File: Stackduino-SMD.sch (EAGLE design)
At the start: 58 parts

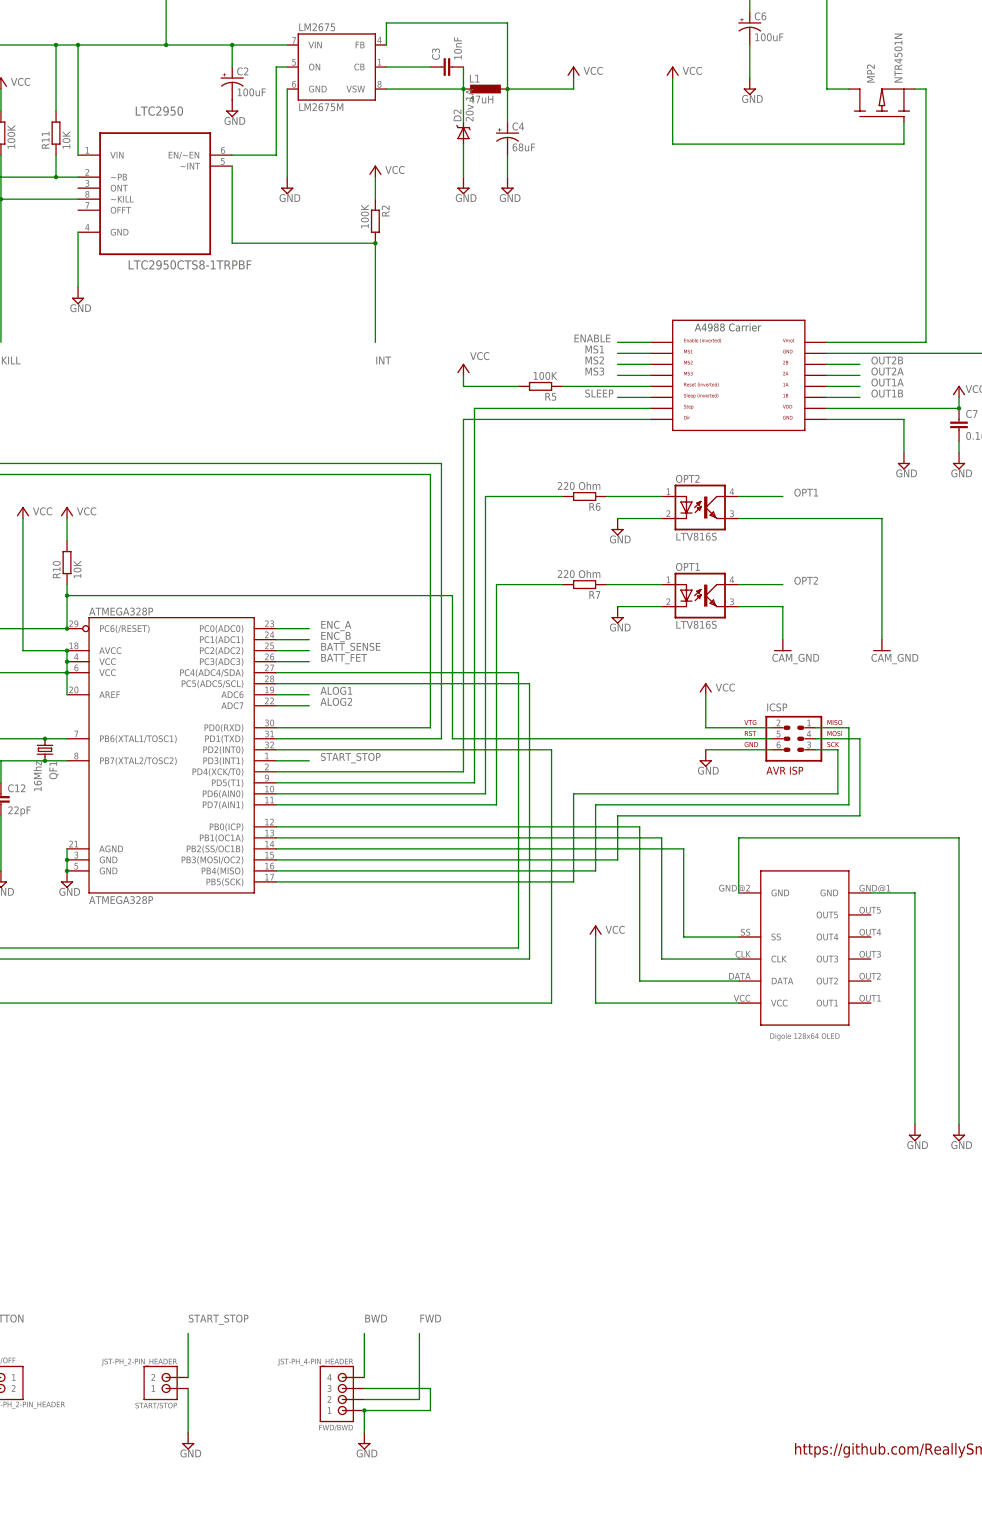
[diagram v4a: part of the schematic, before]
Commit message: reorganised traces to avoid inductor
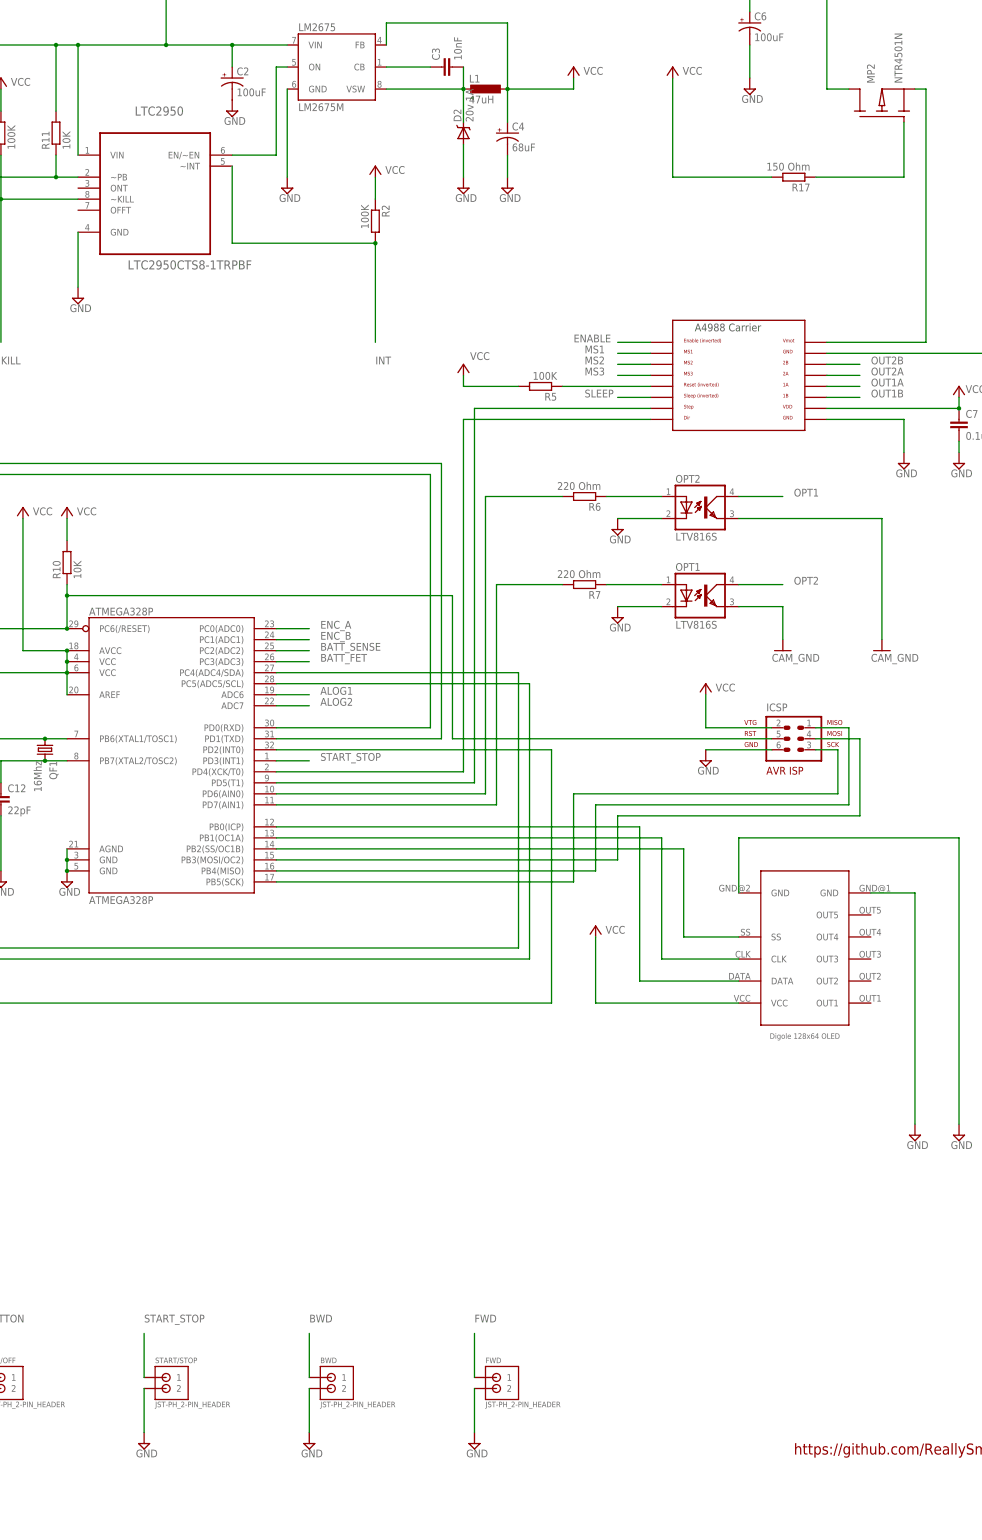
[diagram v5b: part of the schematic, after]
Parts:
- removed FWD/BWD: JST-PH_4-PIN_HEADER, SRG:JST-PH_4-PIN_HEADER
- added BWD, FWD: JST-PH_2-PIN_HEADER, SRG:JST-PH_2-PIN_HEADER
- added R17: 150 Ohm, eagle-ltspice:R
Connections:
- new net N$10: MP2.G, R17.1
- net BWD: now also BWD.1; no longer FWD/BWD.4
- net FWD: now also FWD.1; no longer FWD/BWD.2
- net GND: now also BWD.2, FWD.2, START/STOP.2; no longer FWD/BWD.1, FWD/BWD.3, START/STOP.1
- net START_STOP: now also START/STOP.1; no longer START/STOP.2
- net VCC: now also R17.2; no longer MP2.G
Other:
- moved on the sheet: START/STOP
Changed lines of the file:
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@@
 <part name="SUPPLY29" library="supply2" deviceset="GND" device=""/>
 <part name="SUPPLY30" library="supply2" deviceset="GND" device=""/>
-<part name="SUPPLY33" library="supply2" deviceset="GND" device=""/>
 <part name="SUPPLY35" library="supply2" deviceset="GND" device=""/>
 <part name="SUPPLY36" library="supply2" deviceset="GND" device=""/>
@@
 <part name="ENCODER" library="SRG" deviceset="JST-PH_3-PIN_HEADER" device=""/>
 <part name="MENU_SEL" library="SRG" deviceset="JST-PH_2-PIN_HEADER" device=""/>
-<part name="FWD/BWD" library="SRG" deviceset="JST-PH_4-PIN_HEADER" device=""/>
 <part name="ON/OFF" library="SRG" deviceset="JST-PH_2-PIN_HEADER" device=""/>
 <part name="R1" library="eagle-ltspice" deviceset="R" device="" value="100K"/>
@@
 <part name="CAM_GND2" library="supply1" deviceset="GND" device="" value="CAM_GND"/>
 <part name="FRAME1" library="frames" deviceset="FRAME_C_L" device=""/>
+<part name="BWD" library="SRG" deviceset="JST-PH_2-PIN_HEADER" device=""/>
+<part name="FWD" library="SRG" deviceset="JST-PH_2-PIN_HEADER" device=""/>
+<part name="SUPPLY19" library="supply2" deviceset="GND" device=""/>
+<part name="SUPPLY23" library="supply2" deviceset="GND" device=""/>
+<part name="R17" library="eagle-ltspice" deviceset="R" device="" value="150 Ohm"/>
 </parts>
 <sheets>
@@
 <instance part="ICSP" gate="G$1" x="129.54" y="-17.78"/>
 <instance part="SUPPLY24" gate="GND" x="109.22" y="-22.86"/>
-<instance part="SUPPLY26" gate="GND" x="-10.16" y="-180.34"/>
+<instance part="SUPPLY26" gate="GND" x="-20.32" y="-180.34"/>
 <instance part="SUPPLY27" gate="GND" x="-91.44" y="-180.34"/>
 <instance part="SUPPLY29" gate="GND" x="88.9" y="10.16"/>
 <instance part="SUPPLY30" gate="GND" x="88.9" y="30.48"/>
-<instance part="SUPPLY33" gate="GND" x="30.48" y="-180.34"/>
 <instance part="SUPPLY35" gate="GND" x="-215.9" y="-180.34"/>
 <instance part="SUPPLY36" gate="GND" x="-200.66" y="-180.34"/>
@@
 <instance part="C1" gate="G$1" x="-78.74" y="134.62"/>
 <instance part="GND4" gate="GND" x="-78.74" y="91.44"/>
-<instance part="START/STOP" gate="G$1" x="-17.78" y="-165.1" rot="R180"/>
+<instance part="START/STOP" gate="G$1" x="-12.7" y="-167.64"/>
 <instance part="ENCODER" gate="G$1" x="-99.06" y="-167.64" rot="R180"/>
 <instance part="MENU_SEL" gate="G$1" x="-132.08" y="-167.64"/>
-<instance part="FWD/BWD" gate="G$1" x="22.86" y="-170.18" rot="R180"/>
 <instance part="ON/OFF" gate="G$1" x="-50.8" y="-167.64"/>
 <instance part="R1" gate="G$1" x="-53.34" y="121.92" rot="R90"/>
@@
 <instance part="FRAME1" gate="G$1" x="-325.12" y="-210.82"/>
 <instance part="FRAME1" gate="G$2" x="127" y="-210.82"/>
+<instance part="BWD" gate="G$1" x="25.4" y="-167.64"/>
+<instance part="FWD" gate="G$1" x="63.5" y="-167.64"/>
+<instance part="SUPPLY19" gate="GND" x="17.78" y="-180.34"/>
+<instance part="SUPPLY23" gate="GND" x="55.88" y="-180.34"/>
+<instance part="R17" gate="G$1" x="129.54" y="111.76" rot="R180"/>
 </instances>
 <busses>
@@
 </segment>
 <segment>
-<pinref part="START/STOP" gate="G$1" pin="1"/>
 <pinref part="SUPPLY26" gate="GND" pin="GND"/>
-<wire x1="-10.16" y1="-167.64" x2="-10.16" y2="-177.8" width="0.1524" layer="91"/>
-</segment>
-<segment>
-<pinref part="SUPPLY33" gate="GND" pin="GND"/>
-<pinref part="FWD/BWD" gate="G$1" pin="1"/>
-<wire x1="30.48" y1="-177.8" x2="30.48" y2="-172.72" width="0.1524" layer="91"/>
-<pinref part="FWD/BWD" gate="G$1" pin="3"/>
-<wire x1="30.48" y1="-167.64" x2="45.72" y2="-167.64" width="0.1524" layer="91"/>
-<wire x1="45.72" y1="-167.64" x2="45.72" y2="-172.72" width="0.1524" layer="91"/>
-<wire x1="45.72" y1="-172.72" x2="30.48" y2="-172.72" width="0.1524" layer="91"/>
-<junction x="30.48" y="-172.72"/>
+<pinref part="START/STOP" gate="G$1" pin="2"/>
+<wire x1="-20.32" y1="-167.64" x2="-20.32" y2="-177.8" width="0.1524" layer="91"/>
 </segment>
 <segment>
@@
 <wire x1="-208.28" y1="96.52" x2="-208.28" y2="71.12" width="0.1524" layer="91"/>
 <pinref part="SUPPLY13" gate="GND" pin="GND"/>
+</segment>
+<segment>
+<pinref part="SUPPLY19" gate="GND" pin="GND"/>
+<pinref part="BWD" gate="G$1" pin="2"/>
+<wire x1="17.78" y1="-167.64" x2="17.78" y2="-177.8" width="0.1524" layer="91"/>
+</segment>
+<segment>
+<pinref part="SUPPLY23" gate="GND" pin="GND"/>
+<pinref part="FWD" gate="G$1" pin="2"/>
+<wire x1="55.88" y1="-167.64" x2="55.88" y2="-177.8" width="0.1524" layer="91"/>
 </segment>
 </net>
@@
 </segment>
 <segment>
-<pinref part="START/STOP" gate="G$1" pin="2"/>
-<wire x1="-10.16" y1="-154.94" x2="-10.16" y2="-165.1" width="0.1524" layer="91"/>
-<label x="-10.16" y="-152.4" size="1.778" layer="95"/>
+<label x="-20.32" y="-152.4" size="1.778" layer="95"/>
+<pinref part="START/STOP" gate="G$1" pin="1"/>
+<wire x1="-20.32" y1="-165.1" x2="-20.32" y2="-154.94" width="0.1524" layer="91"/>
 </segment>
 </net>
@@
 <net name="FWD" class="0">
 <segment>
-<pinref part="FWD/BWD" gate="G$1" pin="2"/>
-<wire x1="30.48" y1="-170.18" x2="43.18" y2="-170.18" width="0.1524" layer="91"/>
-<wire x1="43.18" y1="-170.18" x2="43.18" y2="-154.94" width="0.1524" layer="91"/>
-<label x="43.18" y="-152.4" size="1.778" layer="95"/>
+<label x="55.88" y="-152.4" size="1.778" layer="95"/>
+<wire x1="55.88" y1="-154.94" x2="55.88" y2="-165.1" width="0.1524" layer="91"/>
+<pinref part="FWD" gate="G$1" pin="1"/>
 </segment>
 <segment>
@@
 </segment>
 <segment>
-<pinref part="FWD/BWD" gate="G$1" pin="4"/>
-<wire x1="30.48" y1="-165.1" x2="30.48" y2="-154.94" width="0.1524" layer="91"/>
-<label x="30.48" y="-152.4" size="1.778" layer="95"/>
+<label x="17.78" y="-152.4" size="1.778" layer="95"/>
+<pinref part="BWD" gate="G$1" pin="1"/>
+<wire x1="17.78" y1="-165.1" x2="17.78" y2="-154.94" width="0.1524" layer="91"/>
 </segment>
 </net>
@@
 </segment>
 <segment>
-<pinref part="MP2" gate="G$1" pin="G"/>
-<wire x1="154.94" y1="119.38" x2="101.6" y2="119.38" width="0.1524" layer="91"/>
-<wire x1="101.6" y1="119.38" x2="101.6" y2="134.62" width="0.1524" layer="91"/>
+<wire x1="101.6" y1="111.76" x2="101.6" y2="134.62" width="0.1524" layer="91"/>
 <pinref part="P+5" gate="1" pin="+5V"/>
-<wire x1="154.94" y1="119.38" x2="154.94" y2="124.46" width="0.1524" layer="91"/>
+<pinref part="R17" gate="G$1" pin="2"/>
+<wire x1="124.46" y1="111.76" x2="101.6" y2="111.76" width="0.1524" layer="91"/>
 </segment>
 </net>
@@
 </segment>
 </net>
+<net name="N$10" class="0">
+<segment>
+<pinref part="MP2" gate="G$1" pin="G"/>
+<pinref part="R17" gate="G$1" pin="1"/>
+<wire x1="134.62" y1="111.76" x2="154.94" y2="111.76" width="0.1524" layer="91"/>
+<wire x1="154.94" y1="111.76" x2="154.94" y2="124.46" width="0.1524" layer="91"/>
+</segment>
+</net>

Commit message: added camera input
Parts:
- removed DIG_INPUT: JST-PH_2-PIN_HEADER, SRG:JST-PH_2-PIN_HEADER
- added CAM: JST-PH_3-PIN_HEADER, SRG:JST-PH_3-PIN_HEADER
- added DIG_IO: JST-PH_2-PIN_HEADER, SRG:JST-PH_2-PIN_HEADER
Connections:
- net CAM_GND: now also CAM.3
- net EXTRA_INPUT: now also DIG_IO.1; no longer DIG_INPUT.1
- net GND: now also DIG_IO.2; no longer DIG_INPUT.2
- net OPT1: now also CAM.2
- net OPT2: now also CAM.1
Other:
- moved on the sheet: BWD, DB15, ENCODER, FWD, MENU_SEL, ON/OFF, START/STOP

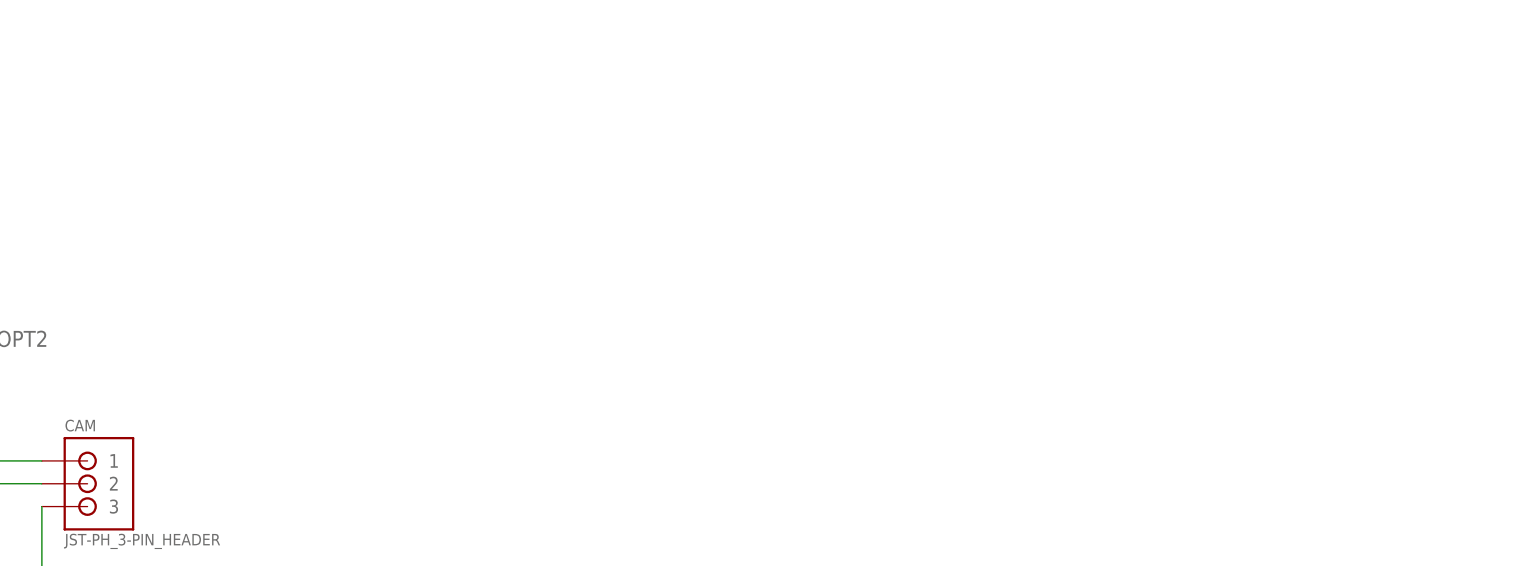
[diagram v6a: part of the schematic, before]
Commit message: Beginning to re-layout traces on grid
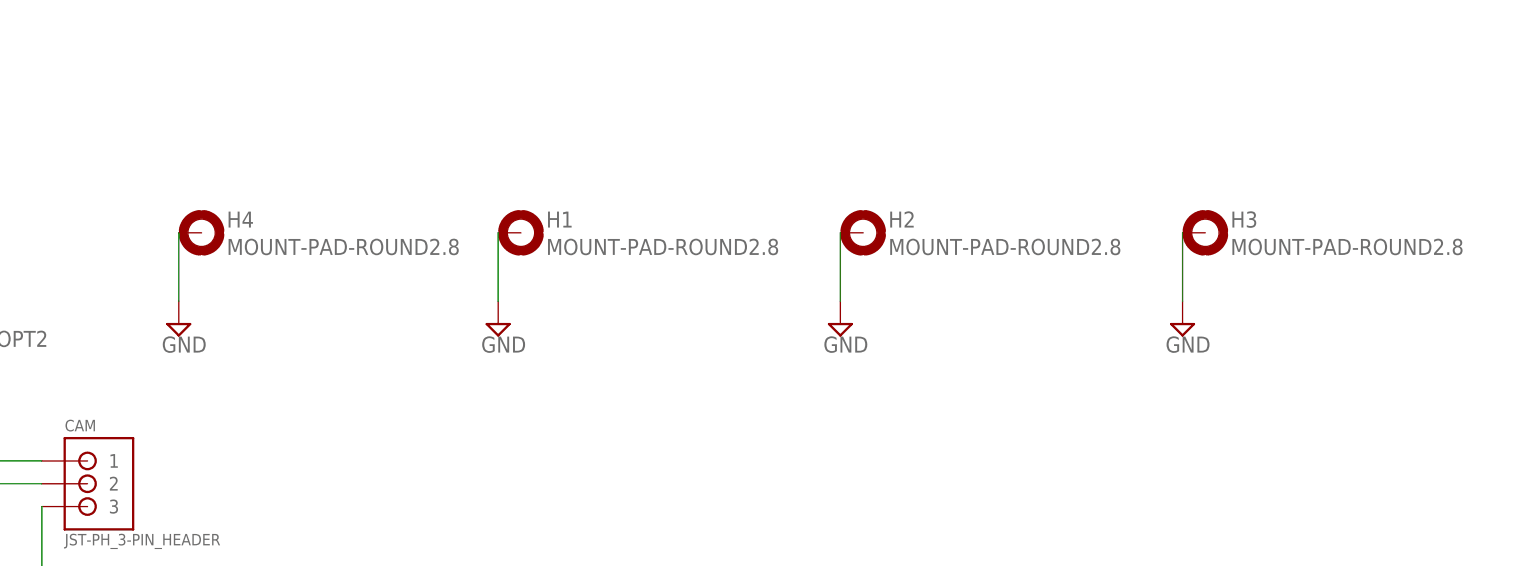
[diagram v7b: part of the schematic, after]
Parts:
- added H1, H2, H3, H4: MOUNT-PAD-ROUND2.8, holes:MOUNT-PAD-ROUND2.8
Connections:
- net GND: now also H1.MOUNT, H2.MOUNT, H3.MOUNT, H4.MOUNT
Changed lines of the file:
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@@
 <part name="CAM" library="SRG" deviceset="JST-PH_3-PIN_HEADER" device=""/>
 <part name="CAM_GND3" library="supply1" deviceset="GND" device="" value="CAM_GND"/>
+<part name="H1" library="holes" deviceset="MOUNT-PAD-ROUND" device="2.8"/>
+<part name="H2" library="holes" deviceset="MOUNT-PAD-ROUND" device="2.8"/>
+<part name="H3" library="holes" deviceset="MOUNT-PAD-ROUND" device="2.8"/>
+<part name="H4" library="holes" deviceset="MOUNT-PAD-ROUND" device="2.8"/>
+<part name="SUPPLY28" library="supply2" deviceset="GND" device=""/>
+<part name="SUPPLY31" library="supply2" deviceset="GND" device=""/>
+<part name="SUPPLY32" library="supply2" deviceset="GND" device=""/>
+<part name="SUPPLY33" library="supply2" deviceset="GND" device=""/>
 </parts>
 <sheets>
@@
 <instance part="CAM" gate="G$1" x="68.58" y="-167.64"/>
 <instance part="CAM_GND3" gate="1" x="63.5" y="-182.88"/>
+<instance part="H1" gate="G$1" x="116.84" y="-139.7"/>
+<instance part="H2" gate="G$1" x="154.94" y="-139.7"/>
+<instance part="H3" gate="G$1" x="193.04" y="-139.7"/>
+<instance part="H4" gate="G$1" x="81.28" y="-139.7"/>
+<instance part="SUPPLY28" gate="GND" x="78.74" y="-149.86"/>
+<instance part="SUPPLY31" gate="GND" x="114.3" y="-149.86"/>
+<instance part="SUPPLY32" gate="GND" x="152.4" y="-149.86"/>
+<instance part="SUPPLY33" gate="GND" x="190.5" y="-149.86"/>
 </instances>
 <busses>
@@
 <wire x1="17.78" y1="-167.64" x2="17.78" y2="-177.8" width="0.1524" layer="91"/>
 </segment>
-</net>
+<segment>
+<pinref part="SUPPLY28" gate="GND" pin="GND"/>
+<wire x1="78.74" y1="-147.32" x2="78.74" y2="-139.7" width="0.1524" layer="91"/>
+<pinref part="H4" gate="G$1" pin="MOUNT"/>
+</segment>
+<segment>
+<pinref part="SUPPLY31" gate="GND" pin="GND"/>
+<pinref part="H1" gate="G$1" pin="MOUNT"/>
+<wire x1="114.3" y1="-147.32" x2="114.3" y2="-139.7" width="0.1524" layer="91"/>
+</segment>
+<segment>
+<pinref part="SUPPLY32" gate="GND" pin="GND"/>
+<pinref part="H2" gate="G$1" pin="MOUNT"/>
+<wire x1="152.4" y1="-147.32" x2="152.4" y2="-139.7" width="0.1524" layer="91"/>
+</segment>
+<segment>
+<pinref part="SUPPLY33" gate="GND" pin="GND"/>
+<pinref part="H3" gate="G$1" pin="MOUNT"/>
+<wire x1="190.5" y1="-147.32" x2="190.5" y2="-139.7" width="0.1524" layer="91"/>
+</segment>
+</net>

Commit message: latest progress on brd v2.1
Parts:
- removed BWD, FWD, MENU_SEL: JST-PH_2-PIN_HEADER, SRG:JST-PH_2-PIN_HEADER
- removed ENCODER: JST-PH_3-PIN_HEADER, SRG:JST-PH_3-PIN_HEADER
- removed ICSP: AVR-ISP-6, avr-5:AVR-ISP-6
- added CON1: B4B-ZR, jst-connectors:B4B-ZR
- added U$1: B5B-ZR, jst-connectors:B5B-ZR
- CAM: value JST-PH_3-PIN_HEADER -> B3B-ZR; device SRG:JST-PH_3-PIN_HEADER -> jst-connectors:B3B-ZR
- U$2: value OLED Display -> B9B-ZR; device Stackduino:DIGOLE_OLED -> jst-connectors:B9B-ZR
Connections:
- removed net N$11: ATMEGA328P.PC6(/RESET), C8.1, ICSP.5, R10.1
- new net +5V: U$2.9
- new net RESET: ATMEGA328P.PC6(/RESET), C8.1, R10.1, U$2.8
- net BWD: now also CON1.1; no longer BWD.1
- net CAM_GND: now also CAM.2; no longer CAM.3
- net ENCSWITCH: now also U$1.5; no longer MENU_SEL.1
- net ENC_A: now also U$1.1; no longer ENCODER.1
- net ENC_B: now also U$1.3; no longer ENCODER.3
- net FWD: now also CON1.3; no longer FWD.1
- net GND: now also CON1.2, CON1.4, U$1.2, U$1.4, U$2.1; no longer BWD.2, ENCODER.2, FWD.2, ICSP.6, MENU_SEL.2, U$2.GND@1, U$2.GND@2
- net MISO: now also U$2.6; no longer ICSP.1
- net MOSI: now also U$2.5; no longer ICSP.4
- net N$22: now also U$2.4; no longer U$2.SS
- net N$23: now also U$2.2; no longer U$2.DATA
- net N$24: now also U$2.3; no longer U$2.CLK
- net OPT1: now also CAM.3; no longer CAM.2
- net OUT1A: now also A4988_CARRIER.1B; no longer A4988_CARRIER.1A
- net OUT1B: now also A4988_CARRIER.1A; no longer A4988_CARRIER.1B
- net SCK: now also U$2.7; no longer ICSP.3
- net VCC: no longer ICSP.2, U$2.VCC
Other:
- moved on the sheet: CAM
